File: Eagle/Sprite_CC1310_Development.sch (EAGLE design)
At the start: 59 parts

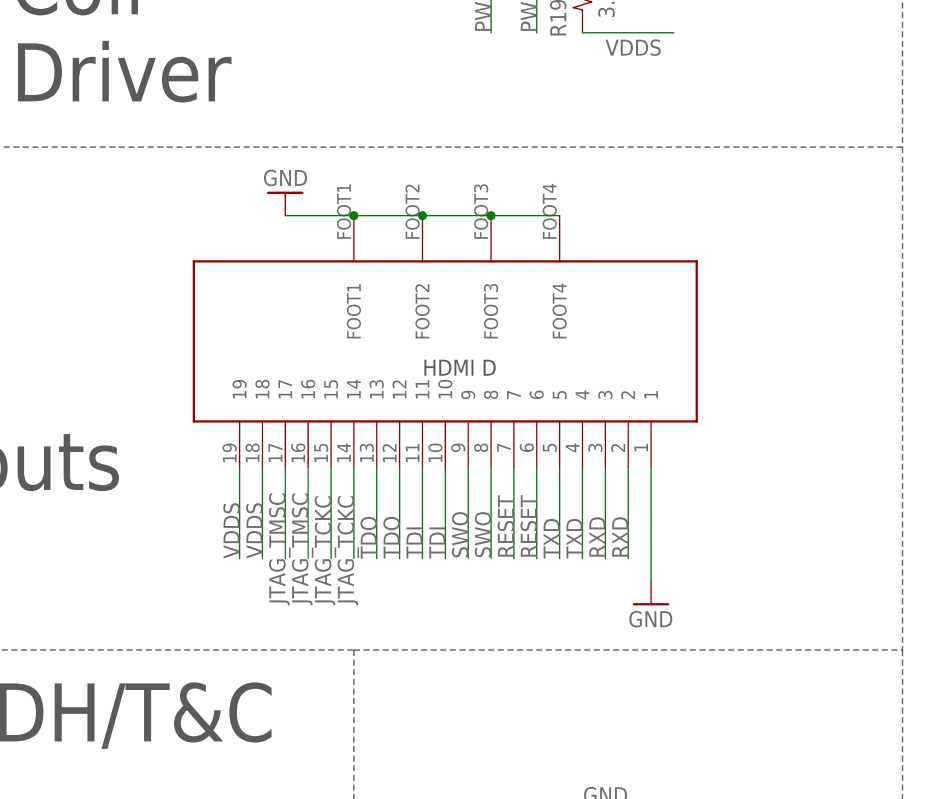
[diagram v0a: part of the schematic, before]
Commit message: updated JTAG and UART pinouts
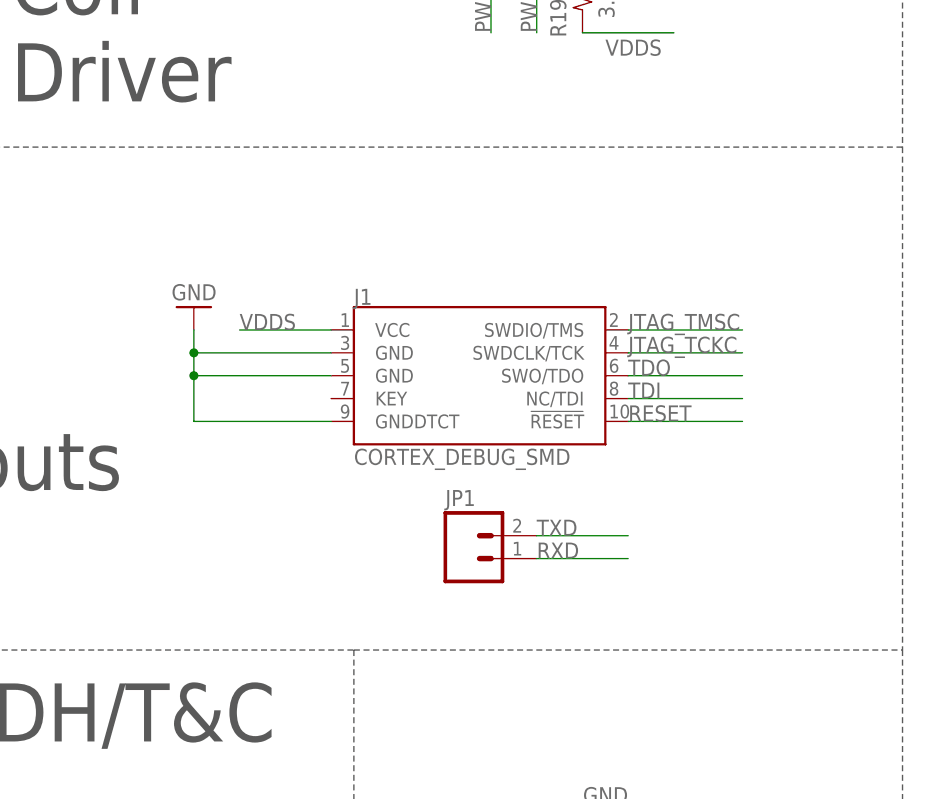
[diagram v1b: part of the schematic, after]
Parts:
- removed U$9: HDMID, HDMID:HDMID
- added J1: CORTEX_DEBUG_SMD, SparkFun-Connectors:CORTEX_DEBUG_SMD
- added JP1: (no value), SparkFun:M02PTH
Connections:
- net GND: now also J1.GND@3, J1.GND@5, J1.GNDDTCT; no longer U$9.1, U$9.FOOT1, U$9.FOOT2, U$9.FOOT3, U$9.FOOT4
- net JTAG_TCKC: now also J1.SWDCLK/TCK; no longer U$9.14, U$9.15
- net JTAG_TMSC: now also J1.SWDIO/TMS; no longer U$9.16, U$9.17
- net RESET: now also J1.!RESET; no longer U$9.6, U$9.7
- net RXD: now also JP1.1; no longer U$9.2, U$9.3
- net SWO: no longer U$9.8, U$9.9
- net TDI: now also J1.NC/TDI; no longer U$9.10, U$9.11
- net TDO: now also J1.SWO/TDO; no longer U$9.12, U$9.13
- net TXD: now also JP1.2; no longer U$9.4, U$9.5
- net VDDS: now also J1.VCC; no longer U$9.18, U$9.19
